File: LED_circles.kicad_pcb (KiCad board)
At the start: 2 copper layers, 125 x 125 mm, 137 parts, among them J1 Conn_ARM_SWD_TagConnect_TC203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, J2 USB_C_Receptacle_PowerOnly_6P, U3 STM32F070CBTx, U74 BD33GA3WEFJ, U75 M95256-WMN6P, U76 M95256-WMN6P

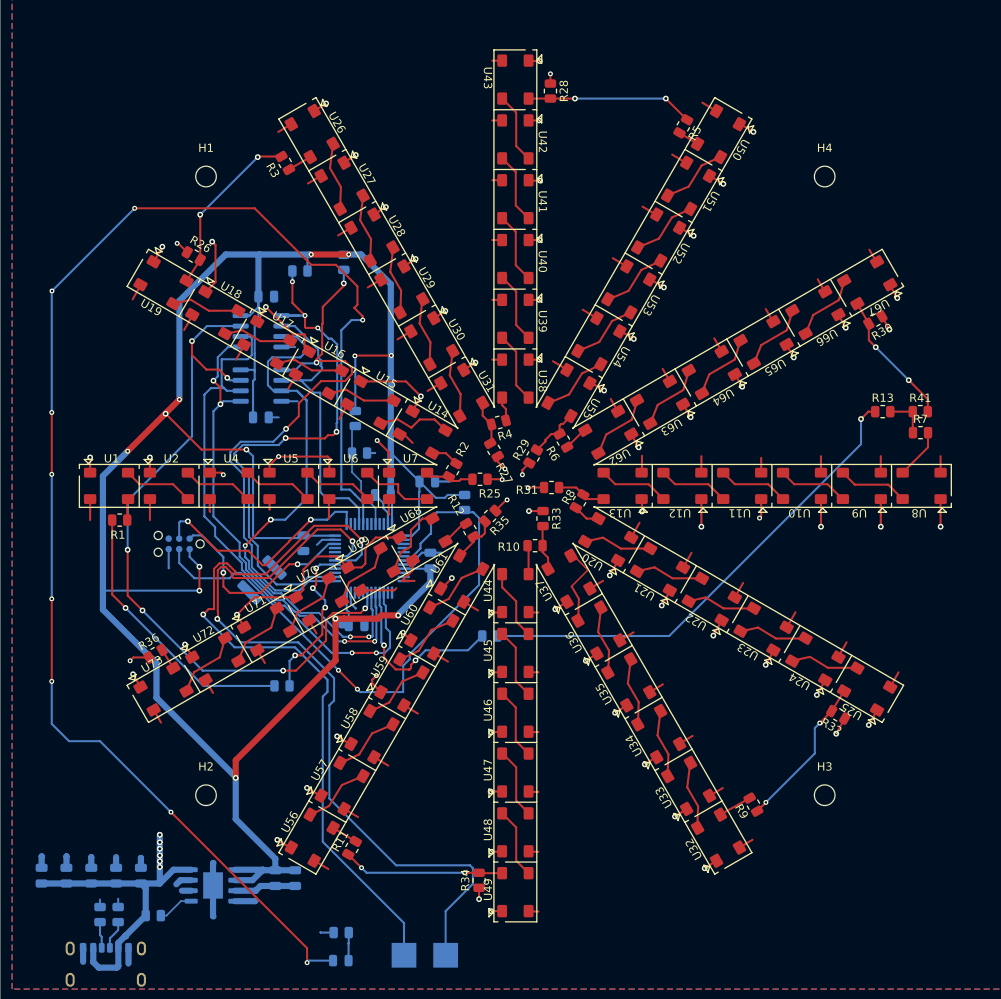
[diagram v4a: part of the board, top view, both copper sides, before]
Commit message: Fixed PCB DRC issues.
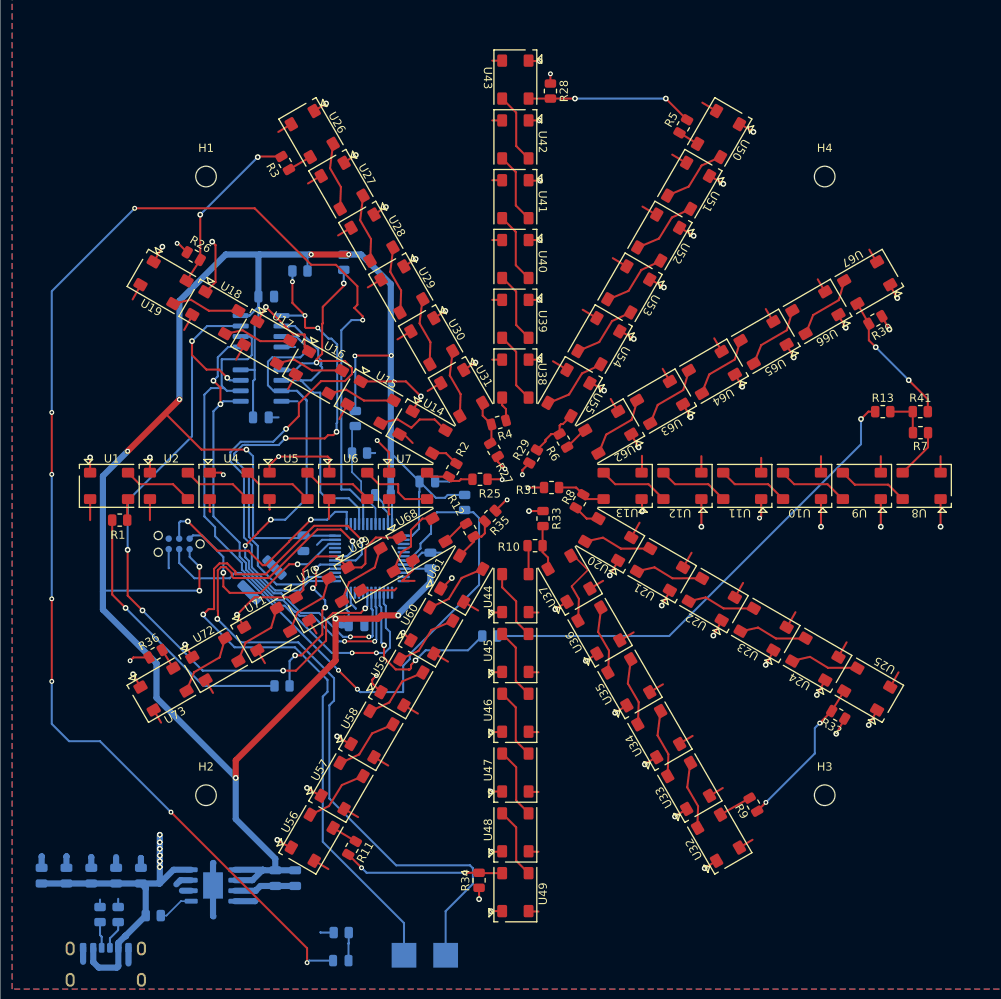
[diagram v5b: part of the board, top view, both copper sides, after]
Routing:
- net /LED_circles_ucontroller/EEPROM2_CS: track 66.9 -> 64.7 mm
- net +3.3V: track 315.6 -> 315.3 mm, vias 13 -> 12
- net Net-(D1-A): track 177.8 -> 177.7 mm, vias 9 -> 8

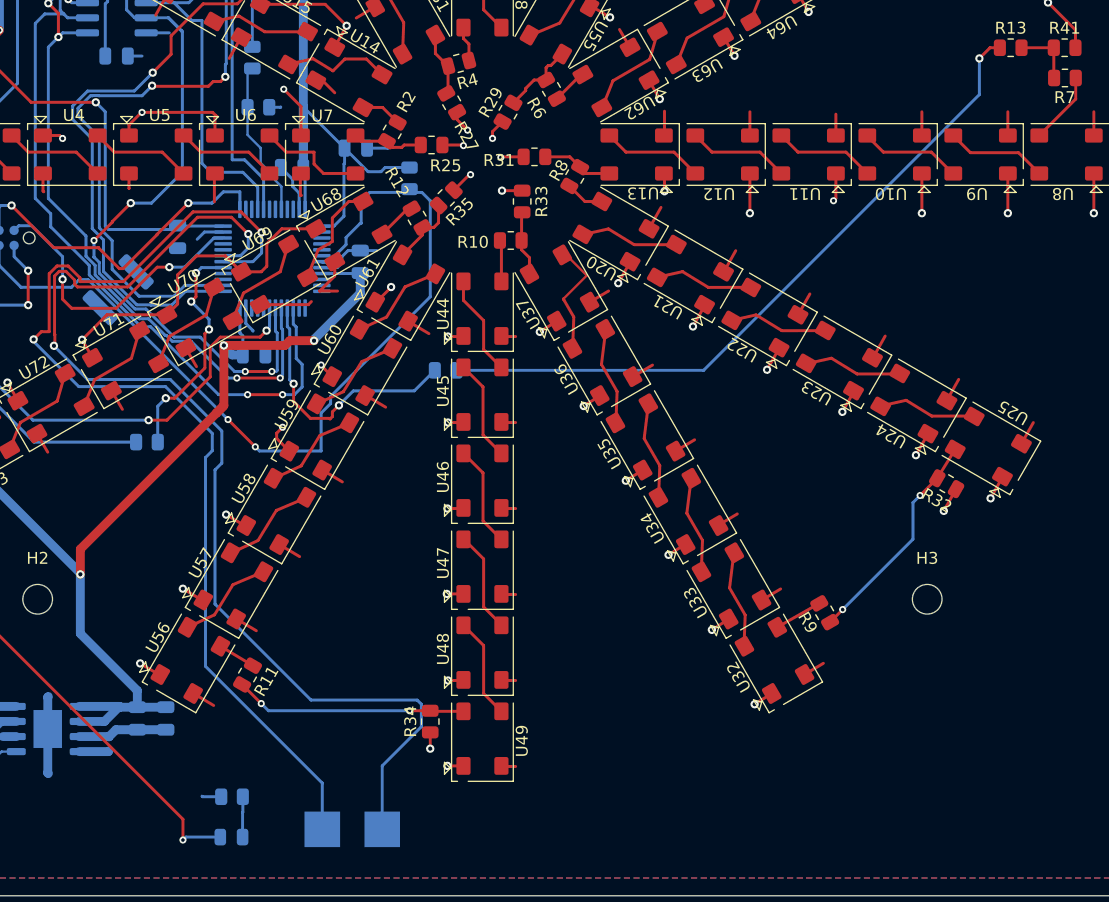
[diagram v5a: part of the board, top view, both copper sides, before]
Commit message: Removed unnecessary jumper resistor
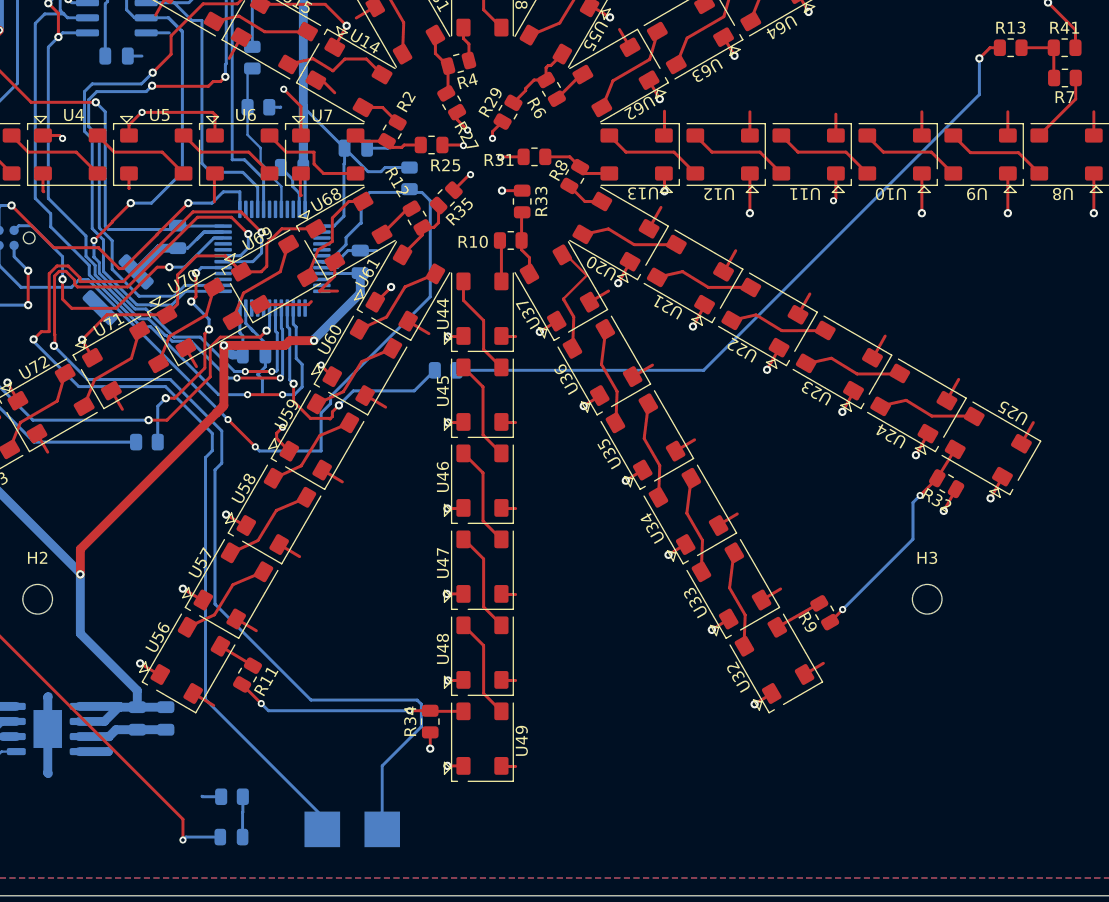
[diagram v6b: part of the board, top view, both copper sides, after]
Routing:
- net GND: track 262.7 -> 276.8 mm
- net /LED_circles_ucontroller/EEPROM2_CS: track 64.7 -> 63.8 mm
- net /LED_circles_ucontroller/EEPROM1_CS: track 69.0 -> 68.3 mm

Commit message: Tweaks
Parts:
- removed R14: 0, Resistor_SMD:R_1812_4532Metric
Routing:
- net /LED_circles_ucontroller/SPI1_SCK: track 68.3 -> 69.4 mm, vias 2 -> 4
- net /LED_circles_ucontroller/SPI1_MOSI: track 59.4 -> 60.3 mm, vias 4 -> 5
- net /LED_circles_ucontroller/WRITE_PROTECT: track 67.6 -> 68.2 mm
- net +3.3V: vias 12 -> 14

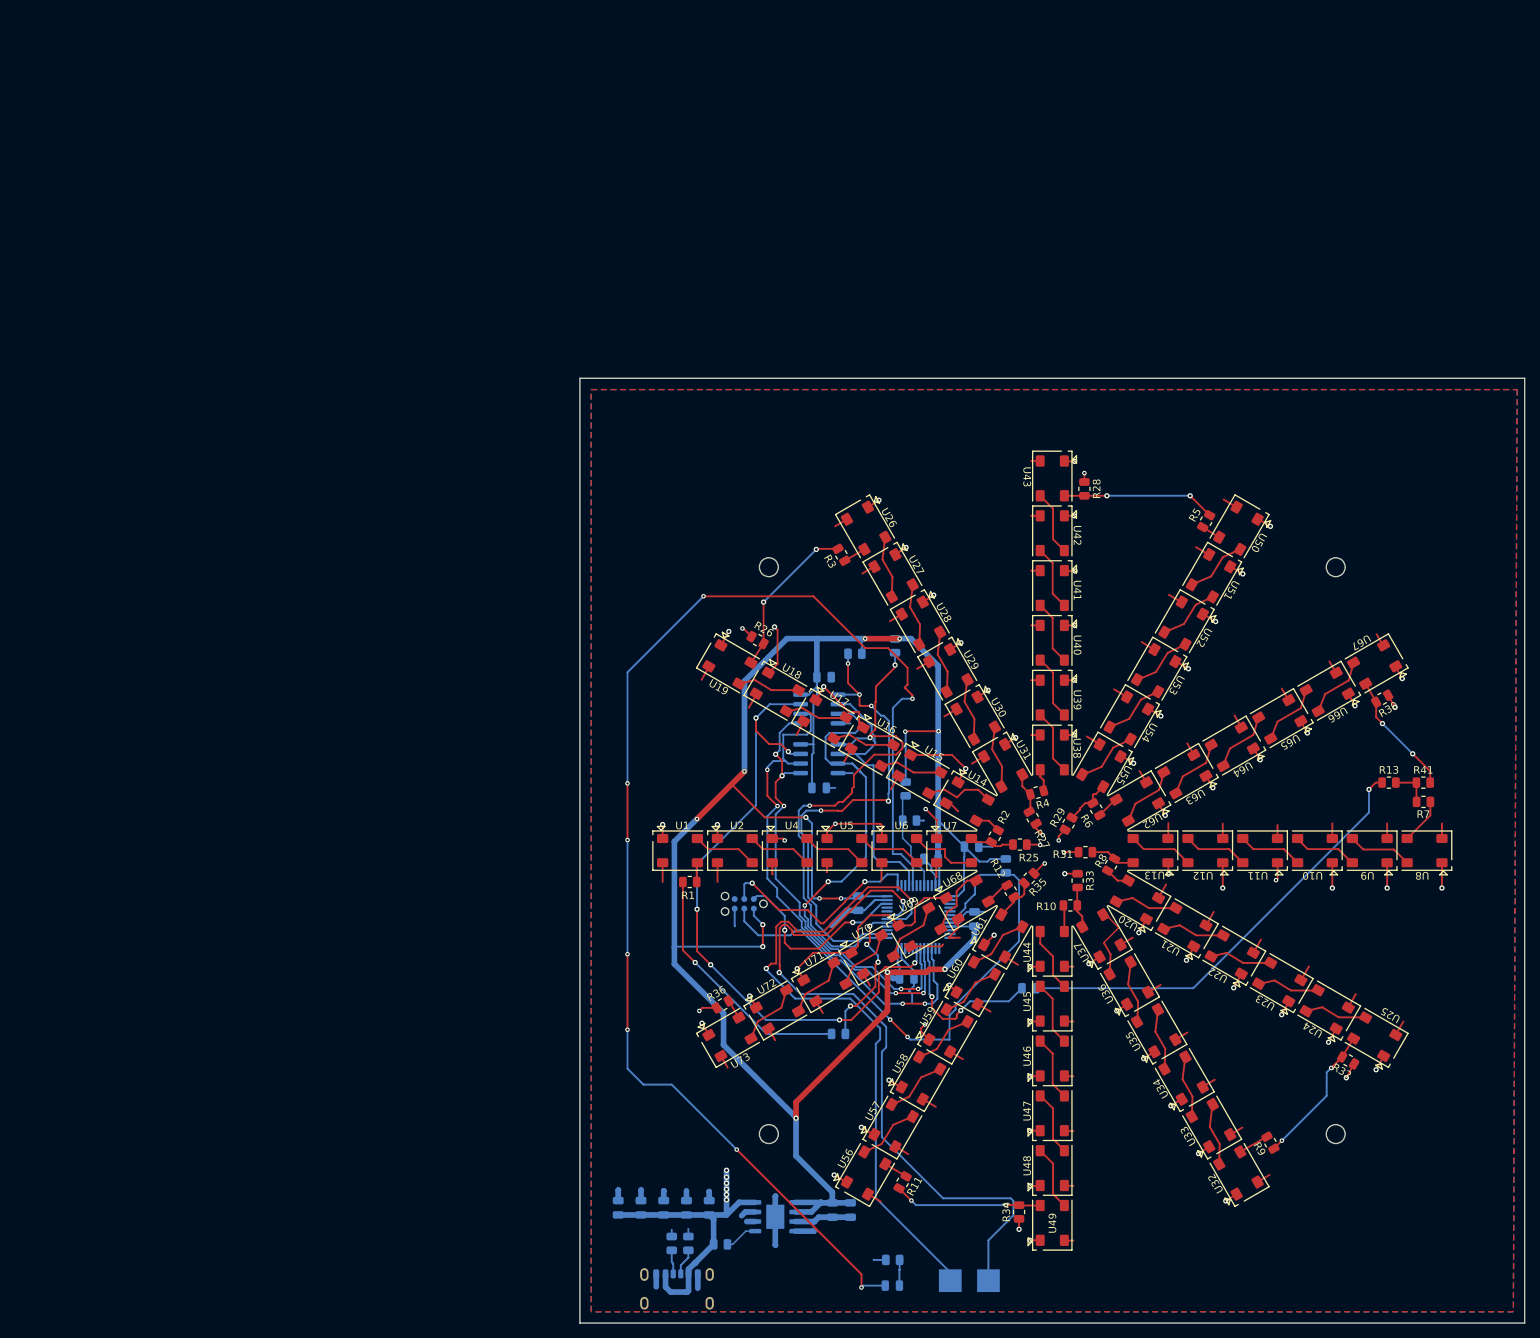
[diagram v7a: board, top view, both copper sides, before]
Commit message: Changed micro controller to larger package
- Also changed PCB DRC to work with OSH Park
- Changed SWD connection to generic  0.1" pogopin headers
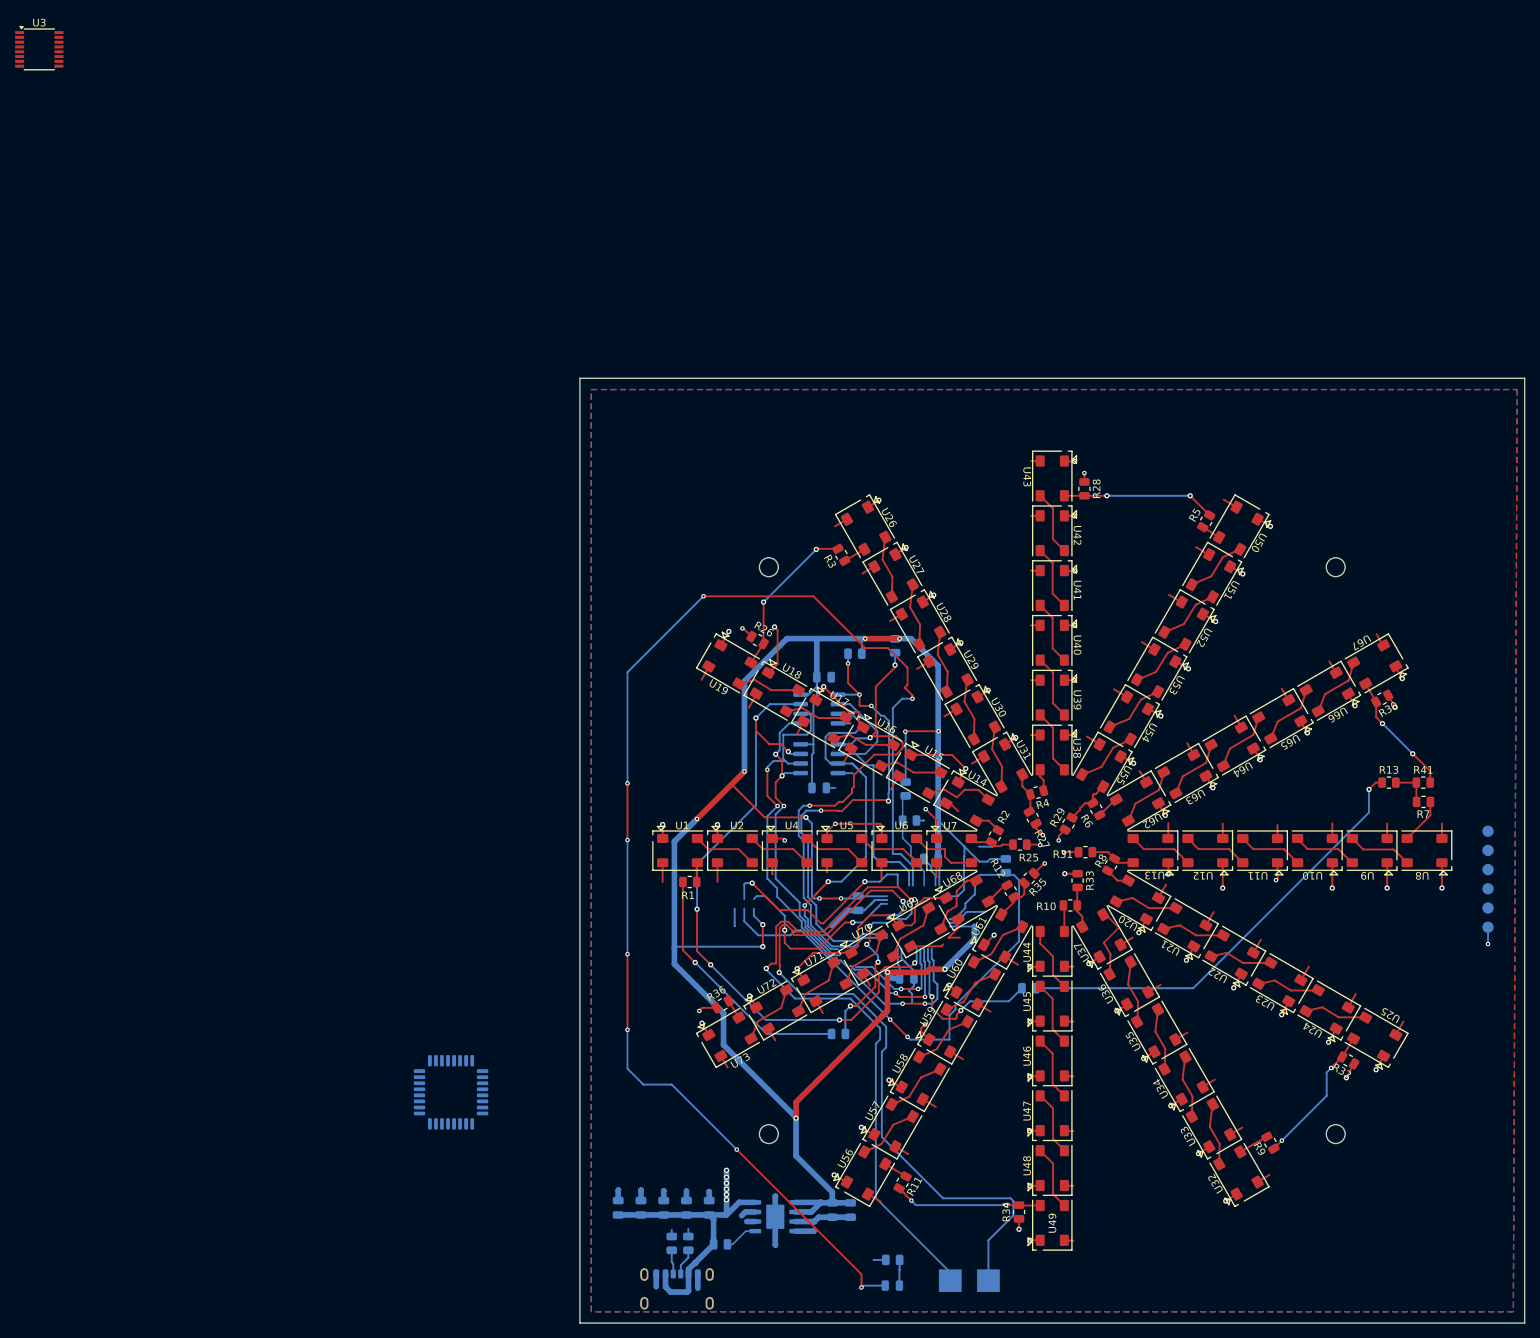
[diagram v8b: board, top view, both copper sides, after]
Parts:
- removed C14, C9: .1uF, Capacitor_SMD:C_0805_2012Metric
- added U77: STM32G071KBTxN, Package_QFP:LQFP-32_7x7mm_P0.8mm, B.Cu at (64.0, 132.0)
- C10: value .1uF -> 1uF
- C11: value .1uF -> 10uF
- J1: value Conn_ARM_SWD_TagConnect_TC2030-NL -> Conn_ARM_SWD_EDGE; footprint Connector:Tag-Connect_TC2030-IDC-NL_2x03_P1.27mm_Vertical -> LED_circles_footprints:ARM_SWD_EDGE
- J2: value USB_C_Receptacle_PowerOnly_6P -> USB_C_Receptacle
- U3: value STM32F070CBTx -> FT230XS; footprint Package_QFP:LQFP-48_7x7mm_P0.5mm -> Package_SO:SSOP-16_3.9x4.9mm_P0.635mm; moved to F.Cu
- moved U3 163.4 mm to (9.47, -6.01), turned to 0 degrees
- moved J1 98.5 mm to (201.2, 103.8), turned to 90 degrees
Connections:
- D1 pad 2: Net-(D1-A) -> unconnected-(D1-A-Pad2)
- J1 pad 4: /LED_circles_ucontroller/SWCLK -> /LED_circles_ucontroller/SWCLK-BOOT0
- J2 pad A5: Net-(J2-CC1) -> unconnected-(J2-CC1-PadA5)
- J2 pad A9: +5V -> Net-(J2-VBUS-PadA4)
- J2 pad B5: Net-(J2-CC2) -> unconnected-(J2-CC2-PadB5)
- J2 pad B9: +5V -> Net-(J2-VBUS-PadA4)
- R38 pad 1: Net-(U3-PA6) -> Net-(U77-PA0)
- R39 pad 1: Net-(U3-PA8) -> Net-(U77-PA8)
- R43 pad 1: Net-(J2-CC2) -> unconnected-(R43-Pad1)
- R44 pad 1: Net-(J2-CC1) -> unconnected-(R44-Pad1)
- TP1 pad 1: /LED_circles_ucontroller/TX -> unconnected-(TP1-Pad1)
- TP2 pad 1: /LED_circles_ucontroller/RX -> unconnected-(TP2-Pad1)
- U3 pad 1: +3.3V -> unconnected-(U3-TXD-Pad1)
- U3 pad 15: /LED_circles_ucontroller/SPI1_SCK -> unconnected-(U3-CBUS0-Pad15)
- U3 pad 16: Net-(U3-PA6) -> unconnected-(U3-CBUS3-Pad16)
- U3 pad 7: Net-(J1-~{RESET}) -> unconnected-(U3-CBUS2-Pad7)
- U3 pad 8: GND -> unconnected-(U3-USBDP-Pad8)
- U3 pad 9: +3.3V -> unconnected-(U3-USBDM-Pad9)
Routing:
- net unconnected-(D1-A-Pad2): track 0.00 -> 177.7 mm, vias 0 -> 8
- net Net-(D1-A): track 177.7 -> 0.00 mm, vias 8 -> 0
- net unconnected-(TP2-Pad1): track 0.00 -> 94.5 mm, vias 0 -> 2
- net /LED_circles_ucontroller/RX: track 94.5 -> 0.00 mm, vias 2 -> 0
- net unconnected-(TP1-Pad1): track 0.00 -> 90.0 mm, vias 0 -> 2
- net /LED_circles_ucontroller/TX: track 90.0 -> 0.00 mm, vias 2 -> 0
- net /LED_circles_ucontroller/SWCLK-BOOT0: track 0.00 -> 28.7 mm, vias 0 -> 2
- net /LED_circles_ucontroller/SWCLK: track 28.7 -> 0.00 mm, vias 2 -> 0
- net Net-(U77-PA0): track 0.00 -> 22.5 mm, vias 0 -> 2
- net Net-(U3-PA6): track 22.5 -> 0.00 mm, vias 2 -> 0
- net Net-(U77-PA8): track 0.00 -> 19.7 mm, vias 0 -> 4
- net Net-(U3-PA8): track 19.7 -> 0.00 mm, vias 4 -> 0
- net (no net): track 0.00 -> 6.74 mm
- net Net-(J2-CC1): track 3.53 -> 0.00 mm
- net /LED_circles_ucontroller/WRITE_PROTECT: track 68.2 -> 64.8 mm
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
